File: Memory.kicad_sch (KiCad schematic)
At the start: 4 parts, among them J1 Micro_SD_Card_Det, U4 X1000

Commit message: Update (Display)
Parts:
- U4: footprint (none) -> TheBrutzlers_Lib:BGA256C80P16X16_1300X1300X130N
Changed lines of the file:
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@@
     (property "Reference" "U4" (id 0) (at 148.59 36.83 0))
     (property "Value" "X1000" (id 1) (at 148.59 39.37 0))
-    (property "Footprint" "" (id 2) (at 125.73 52.07 0)
+    (property "Footprint" "TheBrutzlers_Lib:BGA256C80P16X16_1300X1300X130N" (id 2) (at 125.73 52.07 0)
       (effects (font (size 1.27 1.27)) (justify left) hide)
     )

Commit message: New i.mx6 Version
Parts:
- removed U4: X1000, TheBrutzlers_Lib:BGA256C80P16X16_1300X1300X130N, symbol TheBrutzlers_Lib:X1000
- added C? (x7): 100n, Capacitor_SMD:C_0402_1005Metric, symbol Device:C
- added R? (x3): 10K, symbol Device:R
- added R? (x2): 240R, symbol Device:R
- added R? (x2): 1K2, symbol Device:R
- added U? (x3): IMX6UL, TheBrutzlers_Lib:IMX6UL_BGA289, symbol TheBrutzlers_Lib:IMX6UL
- added U?: MT41K256M16TW, Package_BGA:BGA-96_9.0x13.0mm_Layout2x3x16_P0.8mm, symbol Memory_RAM:AS4C256M16D3
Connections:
- net GND: now also C?.2, C?.2, C?.2, C?.2, C?.2, C?.2, C?.2, R?.1, R?.1, R?.1, R?.1, R?.2, R?.2, U?.A9 (VSS), U?.B1 (VSSQ), U?.B3 (VSS), U?.B9 (VSSQ), U?.D1 (VSSQ), U?.D8 (VSSQ), U?.E1 (VSS), U?.E2 (VSSQ), U?.E8 (VSSQ), U?.F9 (VSSQ), U?.G1 (VSSQ), U?.G8 (VSS), U?.G9 (VSSQ), U?.J2 (VSS), U?.J8 (VSS), U?.M1 (VSS), U?.M9 (VSS), U?.P1 (VSS), U?.P9 (VSS), U?.T1 (VSS), U?.T9 (VSS)
- net SD1_DAT2: now reaches J1.1 (DAT2)
- net SD1_DAT2: now also U?.B1 (SD1_DATA2)
- net SD1_DAT3: now reaches J1.2 (DAT3/CD)
- net SD1_DAT3: now also U?.A2 (SD1_DATA3)
- net SD1_CMD: now reaches J1.3 (CMD)
- net SD1_CMD: now also U?.C2 (SD1_CMD)
- net SD1_CLK: now reaches J1.5 (CLK)
- net SD1_CLK: now also U?.C1 (SD1_CLK)
- net SD1_DAT0: now reaches J1.7 (DAT0)
- net SD1_DAT0: now also U?.B3 (SD1_DATA0)
- net SD1_DAT1: now reaches J1.8 (DAT1)
- net SD1_DAT1: now also U?.B2 (SD1_DATA1)
- new net: C?.1, C?.1, C?.1, C?.1, C?.1, C?.1, R?.2, U?.G6 (NVCC_DRAM), U?.H6 (NVCC_DRAM), U?.J6 (NVCC_DRAM), U?.K6 (NVCC_DRAM), U?.L6 (NVCC_DRAM), U?.M6 (NVCC_DRAM)
- new net: R?.1, U?.N4 (DRAM_ZQPAD)
- new net: C?.1, R?.1, R?.2, U?.P4 (DRAM_VREF)
- new net: R?.1, U?.L8 (ZQ)
- new net: U?.A1 (VDDQ), U?.A8 (VDDQ), U?.C1 (VDDQ), U?.C9 (VDDQ), U?.D2 (VDDQ), U?.E9 (VDDQ), U?.F1 (VDDQ), U?.H2 (VDDQ), U?.H9 (VDDQ)
- new net: U?.B2 (VDD), U?.D9 (VDD), U?.G7 (VDD), U?.K2 (VDD), U?.K8 (VDD), U?.N1 (VDD), U?.N9 (VDD), U?.R1 (VDD), U?.R9 (VDD)
- new net MMDC_A0: U?.L5 (DRAM_ADDR00), U?.N3 (A0)
- new net MMDC_A1: U?.H2 (DRAM_ADDR01), U?.P7 (A1)
- new net MMDC_A10: U?.L7 (A10/AP), U?.M4 (DRAM_ADDR10)
- new net MMDC_A11: U?.K3 (DRAM_ADDR11), U?.R7 (A11)
- new net MMDC_A12: U?.L4 (DRAM_ADDR12), U?.N7 (A12/~{BC})
- new net MMDC_A13: U?.H3 (DRAM_ADDR13), U?.T3 (A13)
- new net MMDC_A14: U?.G1 (DRAM_ADDR14), U?.T7 (A14)
- new net MMDC_A15: U?.K5 (DRAM_ADDR15)
- new net MMDC_A2: U?.K1 (DRAM_ADDR02), U?.P3 (A2)
- new net MMDC_A3: U?.M2 (DRAM_ADDR03), U?.N2 (A3)
- new net MMDC_A4: U?.K4 (DRAM_ADDR04), U?.P8 (A4)
- new net MMDC_A5: U?.L1 (DRAM_ADDR05), U?.P2 (A5)
- new net MMDC_A6: U?.G2 (DRAM_ADDR06), U?.R8 (A6)
- new net MMDC_A7: U?.H4 (DRAM_ADDR07), U?.R2 (A7)
- new net MMDC_A8: U?.J4 (DRAM_ADDR08), U?.T8 (A8)
- new net MMDC_A9: U?.L2 (DRAM_ADDR09), U?.R3 (A9)
- new net MMDC_BA0: U?.M1 (DRAM_SDBA0), U?.M2 (BA0)
- new net MMDC_BA1: U?.H1 (DRAM_SDBA1), U?.N8 (BA1)
- new net MMDC_BA2: U?.K2 (DRAM_SDBA2), U?.M3 (BA2)
- new net MMDC_CKE0: R?.2, U?.K9 (CKE), U?.M3 (DRAM_SDCKE0)
- new net MMDC_CKE1: R?.2, U?.J3 (DRAM_SDCKE1)
- new net MMDC_CLKn: U?.K7 (~{CK}), U?.P2 (DRAM_SDCLK0_N)
- new net MMDC_CLKp: U?.J7 (CK), U?.P1 (DRAM_SDCLK0_P)
- new net MMDC_D0: U?.E3 (DQ0), U?.T4 (DRAM_DATA00)
- new net MMDC_D1: U?.F7 (DQ1), U?.U6 (DRAM_DATA01)
- new net MMDC_D10: U?.C8 (DQ10), U?.U5 (DRAM_DATA10)
- new net MMDC_D11: U?.C2 (DQ11), U?.R4 (DRAM_DATA11)
- new net MMDC_D12: U?.A7 (DQ12), U?.P5 (DRAM_DATA12)
- new net MMDC_D13: U?.A2 (DQ13), U?.P3 (DRAM_DATA13)
- new net MMDC_D14: U?.B8 (DQ14), U?.R2 (DRAM_DATA14)
- new net MMDC_D15: U?.A3 (DQ15), U?.R1 (DRAM_DATA15)
- new net MMDC_D2: U?.F2 (DQ2), U?.T6 (DRAM_DATA02)
- new net MMDC_D3: U?.F8 (DQ3), U?.U7 (DRAM_DATA03)
- new net MMDC_D4: U?.H3 (DQ4), U?.U8 (DRAM_DATA04)
- new net MMDC_D5: U?.H8 (DQ5), U?.T8 (DRAM_DATA05)
- new net MMDC_D6: U?.G2 (DQ6), U?.T5 (DRAM_DATA06)
- new net MMDC_D7: U?.H7 (DQ7), U?.U4 (DRAM_DATA07)
- new net MMDC_D8: U?.D7 (DQ8), U?.U2 (DRAM_DATA08)
- new net MMDC_D9: U?.C3 (DQ9), U?.U3 (DRAM_DATA09)
- new net MMDC_ODT: U?.K1 (ODT), U?.N1 (DRAM_ODT0)
- new net MMDC_~{CAS}: U?.J2 (DRAM_CAS_B), U?.K3 (~{CAS})
- new net MMDC_~{CS1}: U?.H5 (DRAM_CS1_B)
- new net MMDC_~{CS}: U?.L2 (~{CS}), U?.N2 (DRAM_CS0_B)
- new net MMDC_~{RAS}: U?.J3 (~{RAS}), U?.M5 (DRAM_RAS_B)
- new net MMDC_~{RST}: R?.2, U?.G4 (DRAM_RESET), U?.T2 (~{RESET})
- new net MMDC_~{WE}: U?.J1 (DRAM_SDWE_B), U?.L3 (~{WE})
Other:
- note added: "The DDR3 interface is one of the most critical interfaces for chip routing. It must have a 50 Ω controlled impedance for the single-ended traces, and 100 Ω for the differential pairs."

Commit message: Need Rev Platinenmacher
Commit 4 platinenmacher to review and finishing connections
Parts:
- added R?: 240R, symbol Device:R
- added U?: MT41K256M16TW, Package_BGA:BGA-96_9.0x13.0mm_Layout2x3x16_P0.8mm, symbol Memory_RAM:AS4C256M16D3
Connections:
- net GND: now also R?.2, U?.A9 (VSS), U?.B1 (VSSQ), U?.B3 (VSS), U?.B9 (VSSQ), U?.D1 (VSSQ), U?.D8 (VSSQ), U?.E1 (VSS), U?.E2 (VSSQ), U?.E8 (VSSQ), U?.F9 (VSSQ), U?.G1 (VSSQ), U?.G8 (VSS), U?.G9 (VSSQ), U?.J2 (VSS), U?.J8 (VSS), U?.M1 (VSS), U?.M9 (VSS), U?.P1 (VSS), U?.P9 (VSS), U?.T1 (VSS), U?.T9 (VSS)
- net MMDC_A0: now also U?.N3 (A0)
- net MMDC_A1: now also U?.P7 (A1)
- net MMDC_A10: now also U?.L7 (A10/AP)
- net MMDC_A11: now also U?.R7 (A11)
- net MMDC_A12: now also U?.N7 (A12/~{BC})
- net MMDC_A13: now also U?.T3 (A13)
- net MMDC_A14: now also U?.T7 (A14)
- net MMDC_A2: now also U?.P3 (A2)
- net MMDC_A3: now also U?.N2 (A3)
- net MMDC_A4: now also U?.P8 (A4)
- net MMDC_A5: now also U?.P2 (A5)
- net MMDC_A6: now also U?.R8 (A6)
- net MMDC_A7: now also U?.R2 (A7)
- net MMDC_A8: now also U?.T8 (A8)
- net MMDC_A9: now also U?.R3 (A9)
- net MMDC_BA0: now also U?.M2 (BA0)
- net MMDC_BA1: now also U?.N8 (BA1)
- net MMDC_BA2: now also U?.M3 (BA2)
- net MMDC_CKE0: now also U?.K9 (CKE)
- net MMDC_CLKn: now also U?.K7 (~{CK})
- net MMDC_CLKp: now also U?.J7 (CK)
- net MMDC_D0: now also U?.E3 (DQ0)
- net MMDC_D1: now also U?.F7 (DQ1)
- net MMDC_D10: now also U?.C8 (DQ10)
- net MMDC_D11: now also U?.C2 (DQ11)
- net MMDC_D12: now also U?.A7 (DQ12)
- net MMDC_D13: now also U?.A2 (DQ13)
- net MMDC_D14: now also U?.B8 (DQ14)
- net MMDC_D15: now also U?.A3 (DQ15)
- net MMDC_D2: now also U?.F2 (DQ2)
- net MMDC_D3: now also U?.F8 (DQ3)
- net MMDC_D4: now also U?.H3 (DQ4)
- net MMDC_D5: now also U?.H8 (DQ5)
- net MMDC_D6: now also U?.G2 (DQ6)
- net MMDC_D7: now also U?.H7 (DQ7)
- net MMDC_D8: now also U?.D7 (DQ8)
- net MMDC_D9: now also U?.C3 (DQ9)
- net MMDC_ODT: now also U?.K1 (ODT)
- net MMDC_~{CAS}: now also U?.K3 (~{CAS})
- net MMDC_~{CS1}: now also U?.L2 (~{CS})
- net MMDC_~{RAS}: now also U?.J3 (~{RAS})
- net MMDC_~{RST}: now also U?.T2 (~{RESET})
- net MMDC_~{WE}: now also U?.L3 (~{WE})
- net MMDC_~{CS} renamed MMDC_~{CS0}
- new net: U?.A1 (VDDQ), U?.A8 (VDDQ), U?.C1 (VDDQ), U?.C9 (VDDQ), U?.D2 (VDDQ), U?.E9 (VDDQ), U?.F1 (VDDQ), U?.H2 (VDDQ), U?.H9 (VDDQ)
- new net: U?.B2 (VDD), U?.D9 (VDD), U?.G7 (VDD), U?.K2 (VDD), U?.K8 (VDD), U?.N1 (VDD), U?.N9 (VDD), U?.R1 (VDD), U?.R9 (VDD)
- new net: R?.1, U?.L8 (ZQ)
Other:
- note added: "Platinenmacher!"
- moved on the sheet: C?, R?, U?, U?B, U?C, U?H

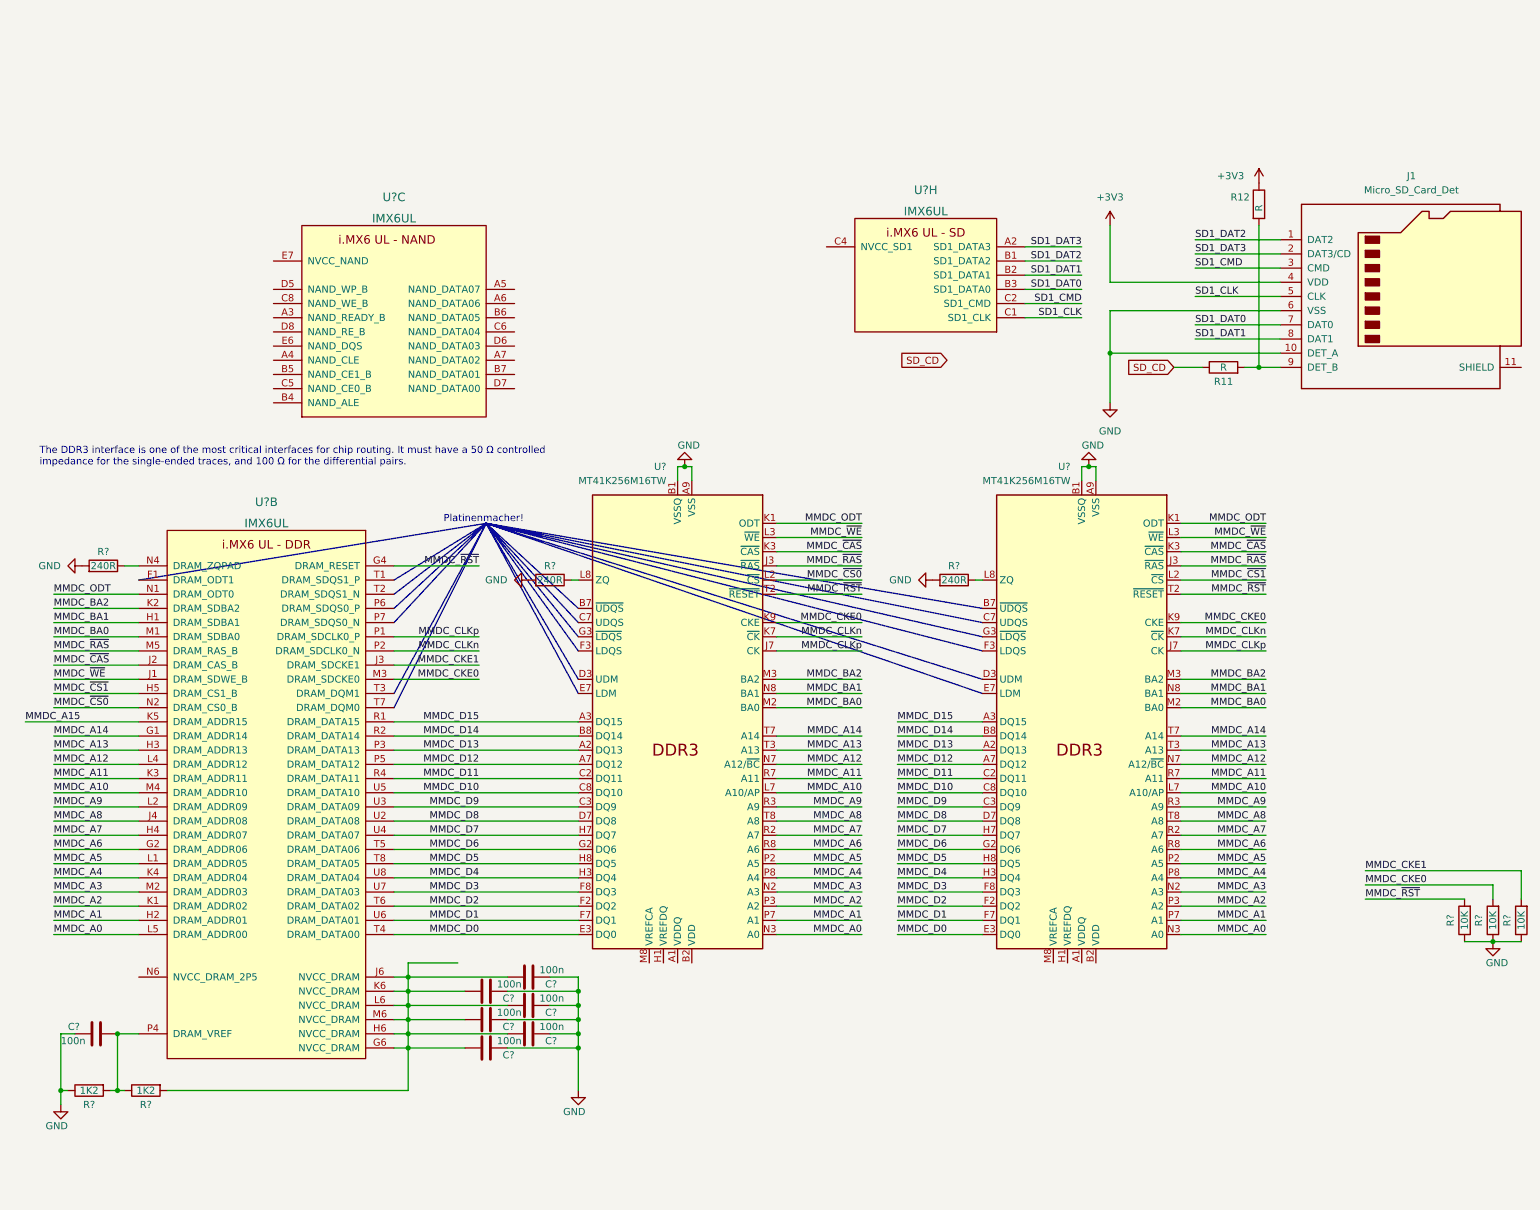
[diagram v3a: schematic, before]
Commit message: Display Update
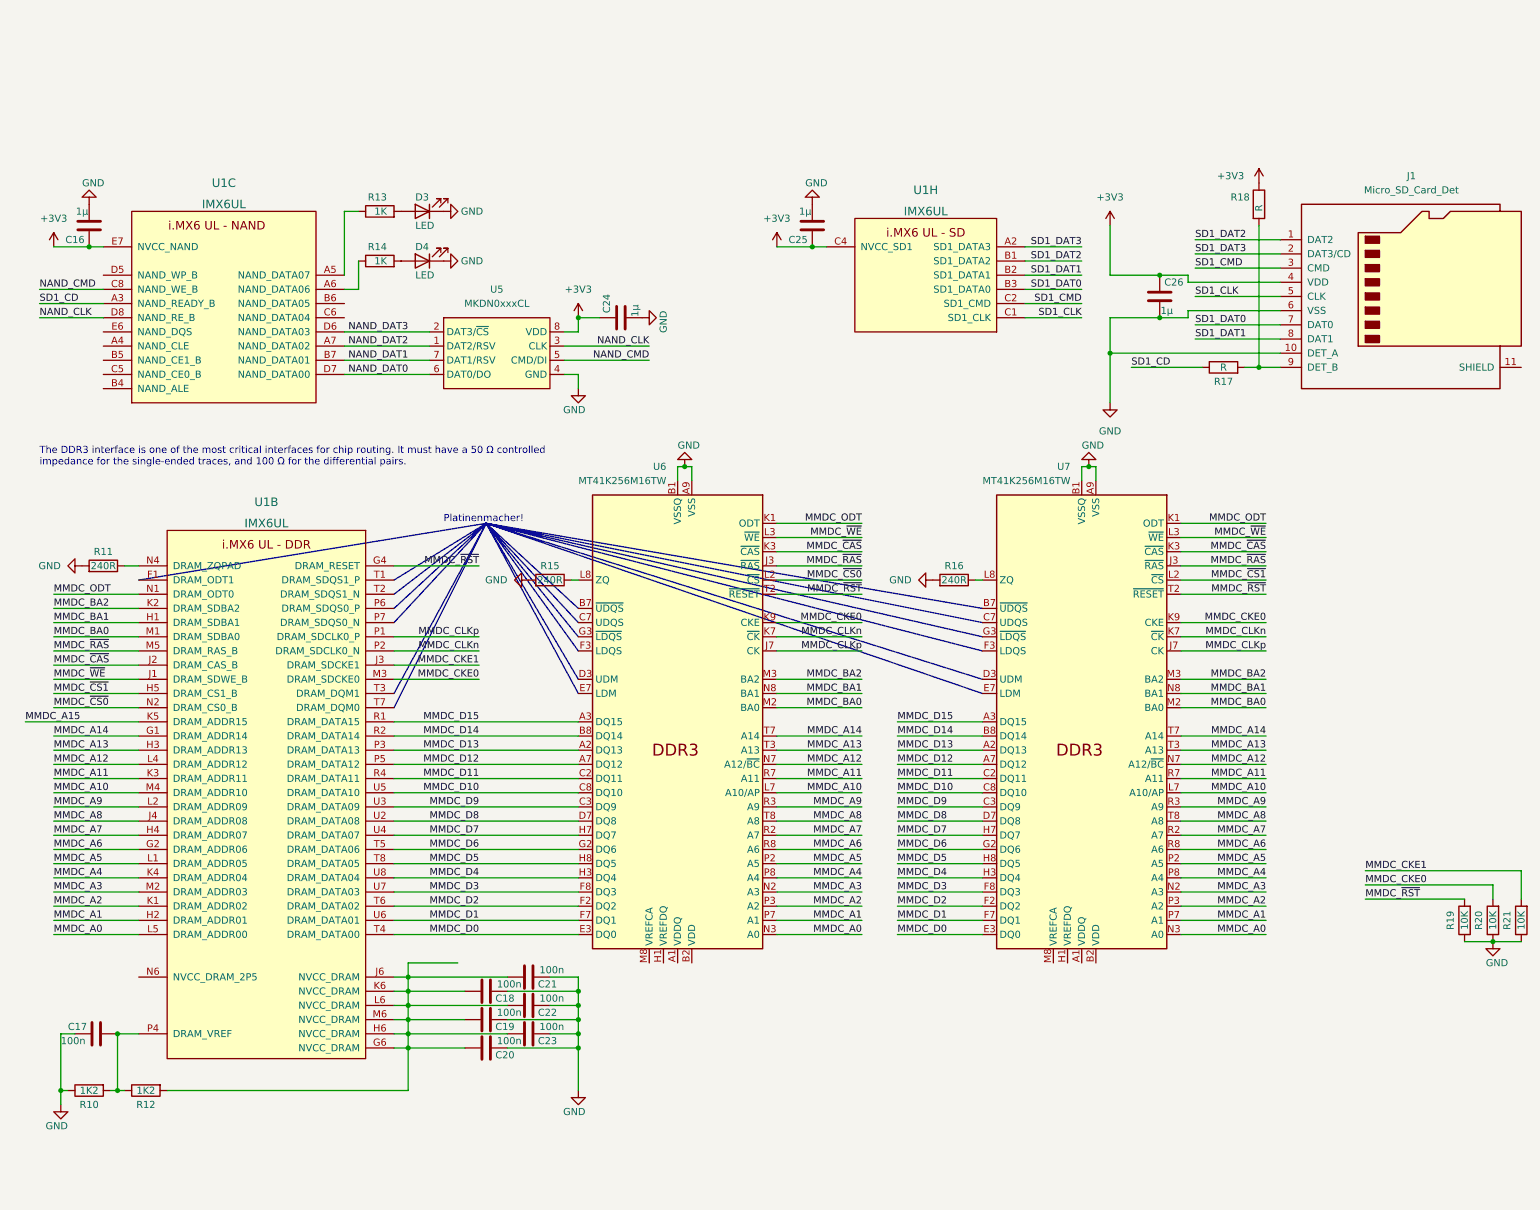
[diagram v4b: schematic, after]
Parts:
- added C16, C24, C25, C26: 1µ, Capacitor_SMD:C_0402_1005Metric, symbol Device:C
- added D3, D4: LED, LED_SMD:LED_0402_1005Metric, symbol Device:LED
- added R13, R14: 1K, Resistor_SMD:R_0402_1005Metric, symbol Device:R
- added U5: MKDN0xxxCL, TheBrutzlers_Lib:LGA-16_NAND, symbol TheBrutzlers_Lib:MKDN0xxxCL
- gave numbers to parts that had none: 18
- renumbered R11 to R17, R12 to R18
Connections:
- net SD_CD is gone; now on net SD1_CD: R17.1
- net +3V3: now also U1.C4 (NVCC_SD1), U1.E7 (NVCC_NAND), C16.1, C24.1, C25.1, C26.1, U5.8 (VDD)
- net GND: now also C16.2, C24.2, C25.2, C26.2, D3.1 (K), D4.1 (K), U5.4 (GND)
- net SD1_CD: now reaches U1.A3 (NAND_READY_B)
- net at U1.A5 (NAND_DATA07): now also R13.1
- net at U1.A6 (NAND_DATA06): now also R14.1
- net NAND_DAT2: now reaches U1.A7 (NAND_DATA02)
- net NAND_DAT2: now also U5.1 (DAT2/RSV)
- net NAND_DAT1: now reaches U1.B7 (NAND_DATA01)
- net NAND_DAT1: now also U5.7 (DAT1/RSV)
- net NAND_CMD: now reaches U1.C8 (NAND_WE_B)
- net NAND_CMD: now also U5.5 (CMD/DI)
- net NAND_DAT3: now reaches U1.D6 (NAND_DATA03)
- net NAND_DAT3: now also U5.2 (DAT3/~{CS})
- net NAND_DAT0: now reaches U1.D7 (NAND_DATA00)
- net NAND_DAT0: now also U5.6 (DAT0/DO)
- net NAND_CLK: now reaches U1.D8 (NAND_RE_B)
- net NAND_CLK: now also U5.3 (CLK)
- new net: D3.2 (A), R13.2
- new net: D4.2 (A), R14.2
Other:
- moved on the sheet: U1C

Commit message: DDR: Review and connection of DDR3 chips
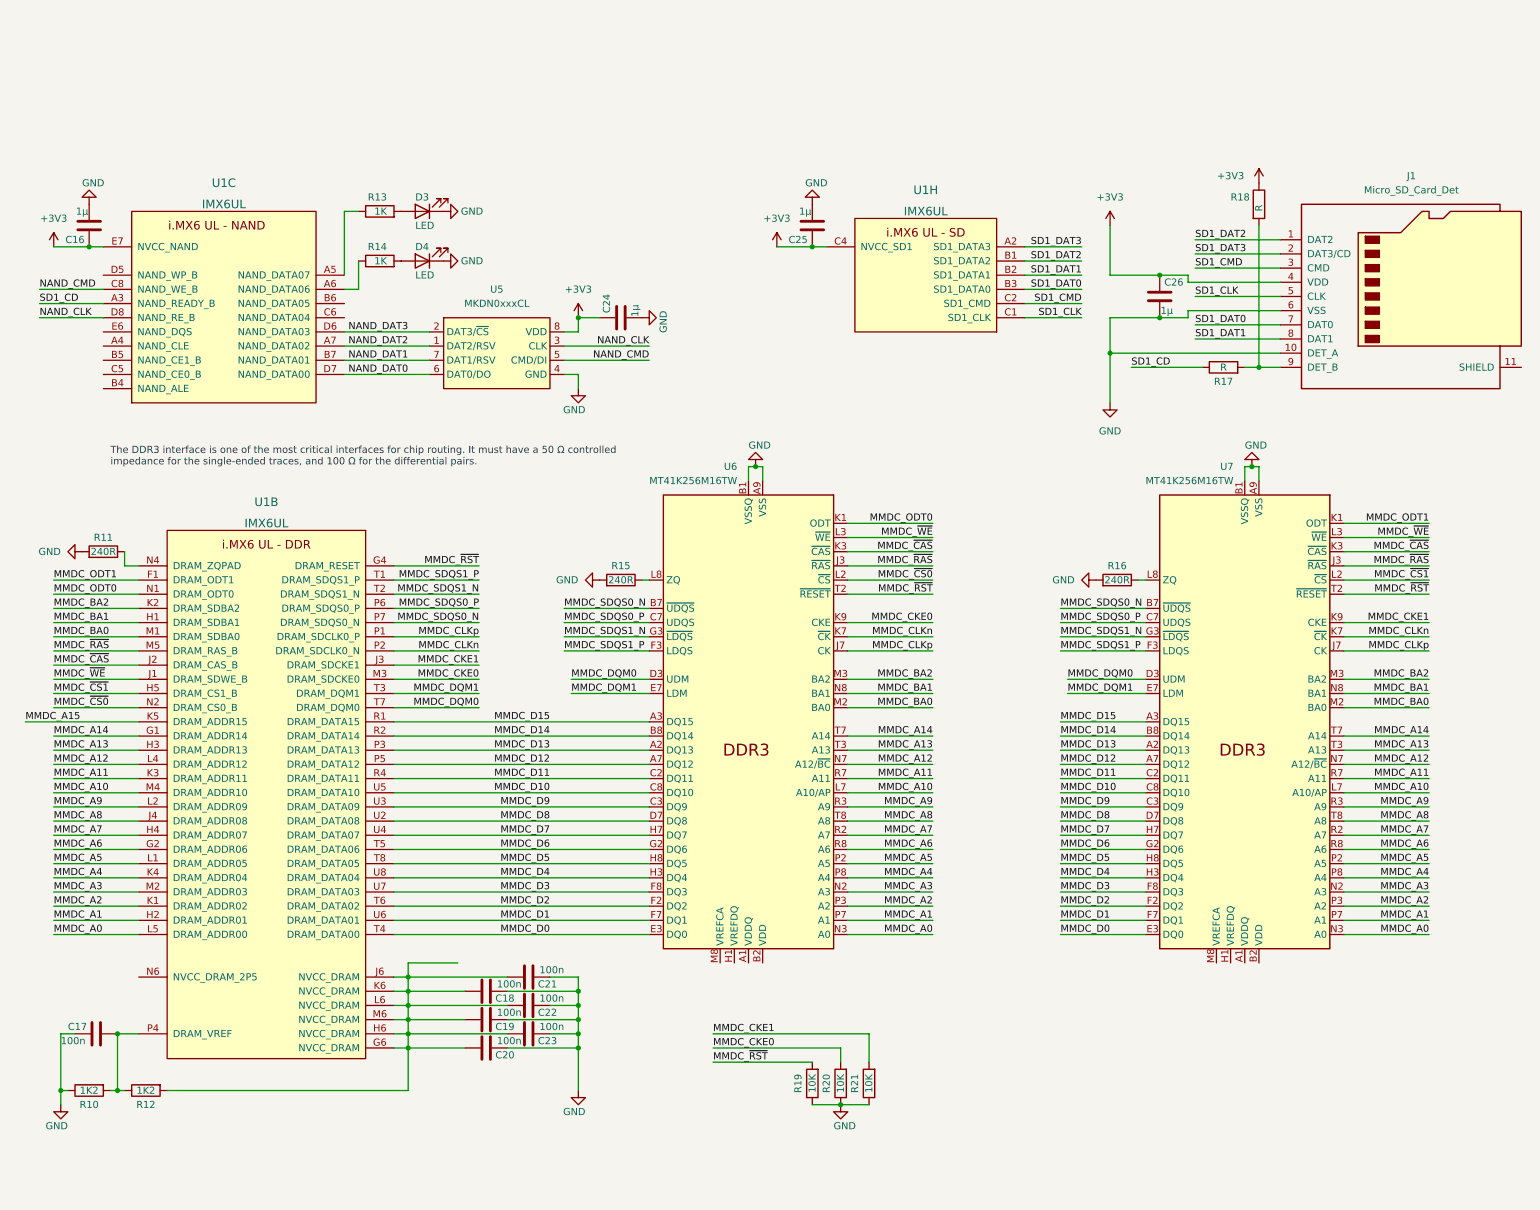
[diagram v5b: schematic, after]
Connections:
- net MMDC_CKE0: no longer U7.K9 (CKE)
- net MMDC_CKE1: now also U7.K9 (CKE)
- net MMDC_ODT1: now reaches U1.F1 (DRAM_ODT1)
- net MMDC_ODT1: now also U7.K1 (ODT)
- net MMDC_SDQS0_P: now reaches U1.P6 (DRAM_SDQS0_P)
- net MMDC_SDQS0_P: now also U6.C7 (UDQS), U7.C7 (UDQS)
- net MMDC_SDQS0_N: now reaches U1.P7 (DRAM_SDQS0_N)
- net MMDC_SDQS0_N: now also U6.B7 (~{UDQS}), U7.B7 (~{UDQS})
- net MMDC_SDQS1_P: now reaches U1.T1 (DRAM_SDQS1_P)
- net MMDC_SDQS1_P: now also U6.F3 (LDQS), U7.F3 (LDQS)
- net MMDC_SDQS1_N: now reaches U1.T2 (DRAM_SDQS1_N)
- net MMDC_SDQS1_N: now also U6.G3 (~{LDQS}), U7.G3 (~{LDQS})
- net MMDC_DQM1: now reaches U1.T3 (DRAM_DQM1)
- net MMDC_DQM1: now also U6.E7 (LDM), U7.E7 (LDM)
- net MMDC_DQM0: now reaches U1.T7 (DRAM_DQM0)
- net MMDC_DQM0: now also U6.D3 (UDM), U7.D3 (UDM)
- net MMDC_ODT renamed MMDC_ODT0
- net MMDC_ODT0: no longer U7.K1 (ODT)
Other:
- note removed: "Platinenmacher!"
- moved on the sheet: R11, R15, R16, R19, R20, R21, U6, U7
